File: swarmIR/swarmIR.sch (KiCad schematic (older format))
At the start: 11 parts, among them Q1 MOSFET_N, U1 TSOP1838, U2 TSOP1838, U3 TSOP1838, U4 TSOP1838

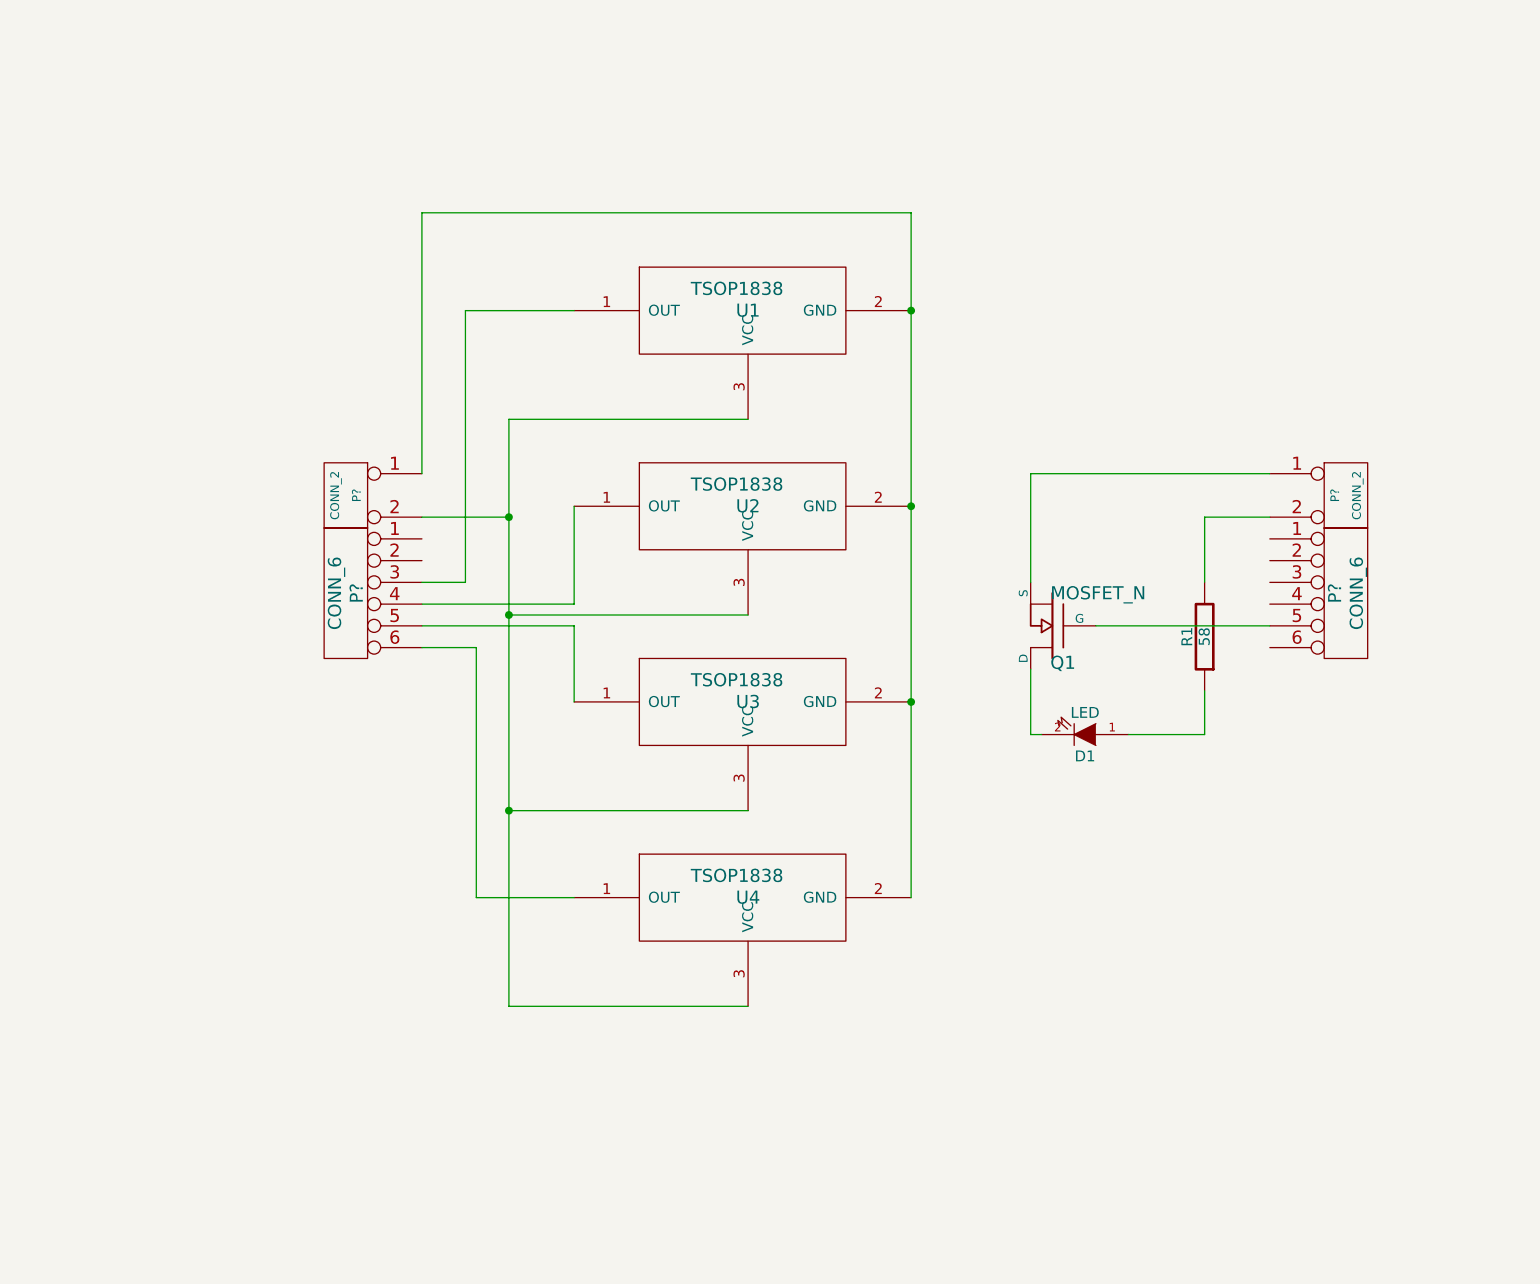
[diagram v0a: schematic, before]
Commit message: added pullups, filter cap & series R
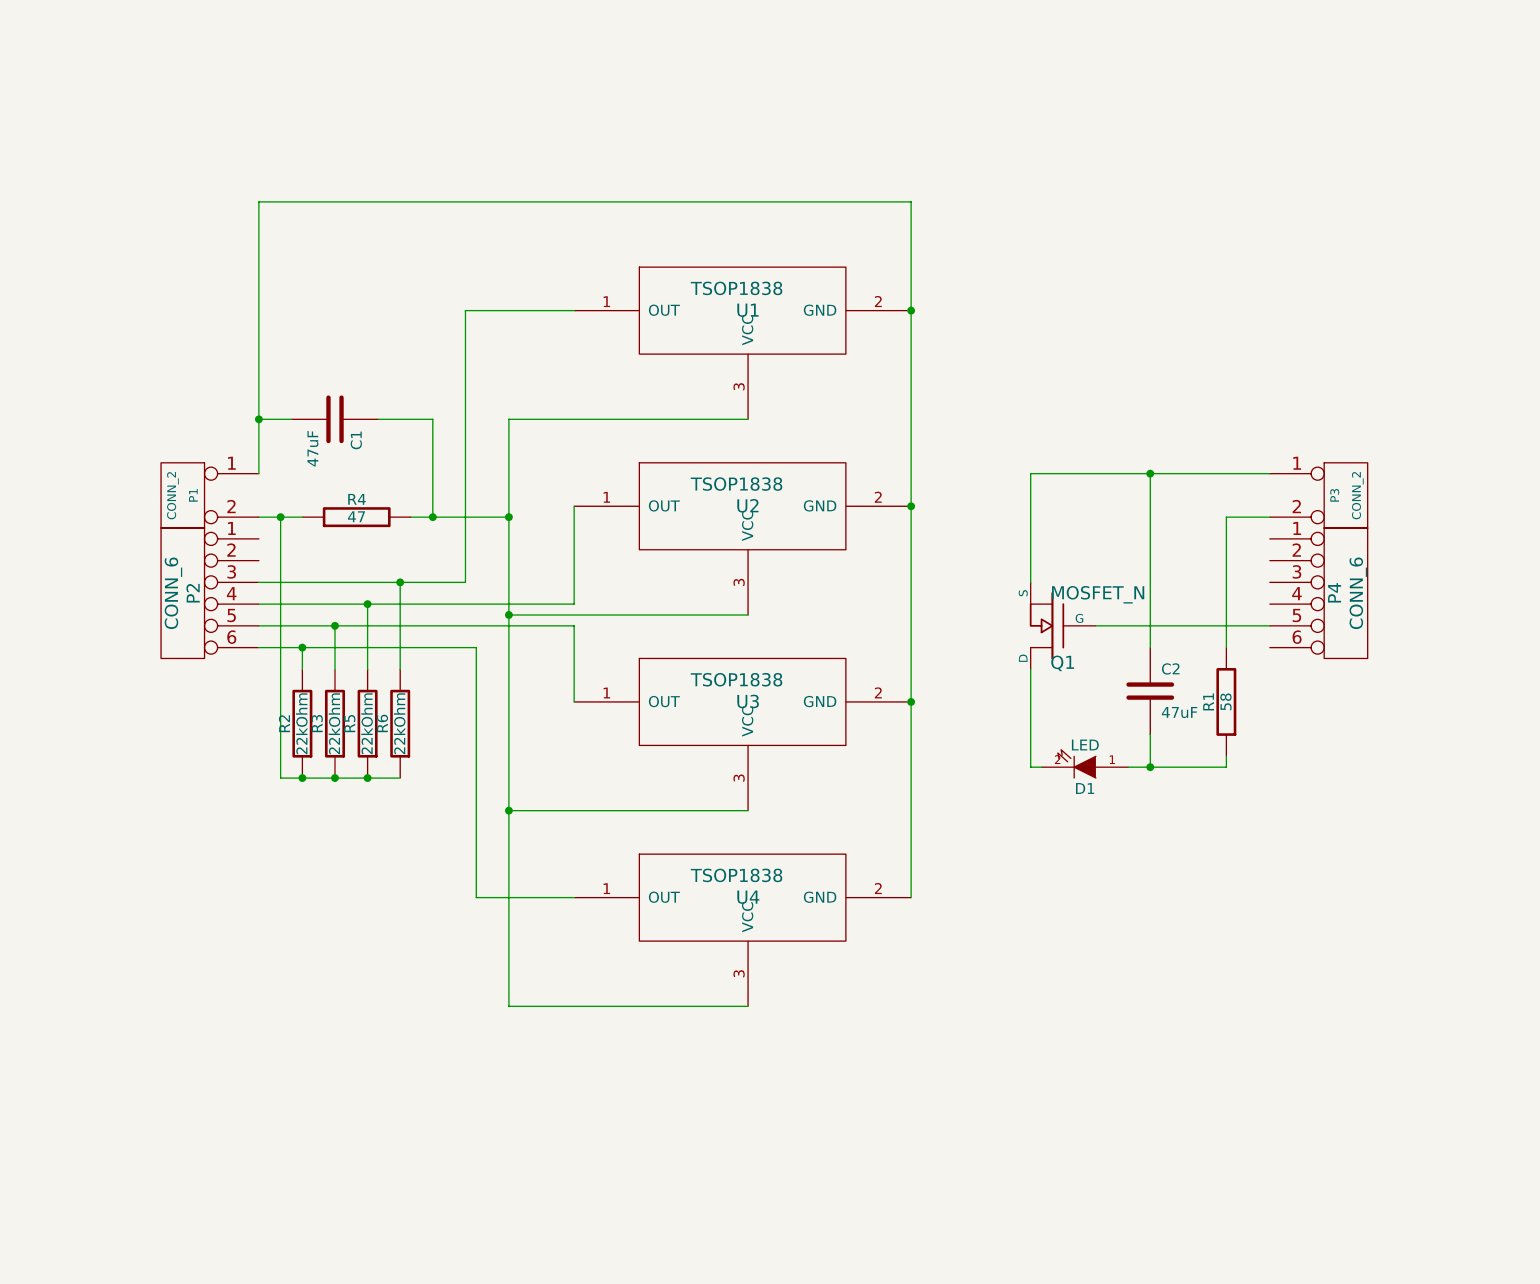
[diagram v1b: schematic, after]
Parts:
- added C1, C2: 47uF, symbol C
- added R2, R3, R5, R6: 22kOhm, symbol R
- added R4: 47, symbol R
- gave numbers to parts that had none: 4
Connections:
- net at P2.3, U1.1 (OUT): now also R6.2
- net at P1.1 (P1), U1.2 (GND), U2.2 (GND)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: now also C1.2
- net at U1.3 (VCC), U2.3 (VCC), U3.3 (VCC)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: now also C1.1, R4.2; no longer P1.2 (PM)
- net at P2.6, U4.1 (OUT): now also R2.2
- net at P2.4, U2.1 (OUT): now also R5.2
- net at P2.5, U3.1 (OUT): now also R3.2
- net at D1.1 (A), R1.1: now also C2.2
- net at P3.1 (P1), Q1.S: now also C2.1
- new net: P1.2 (PM), R2.1, R3.1, R4.1, R5.1, R6.1
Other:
- moved on the sheet: D1, P1, P2, R1
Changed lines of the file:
@@
-EESchema Schematic File Version 2  date Tue 11 Sep 2012 10:58:22 PM CST
+EESchema Schematic File Version 2  date Fri 12 Oct 2012 10:54:19 CST
 LIBS:power
 LIBS:device
@@
 LIBS:atmega32u4
 LIBS:swarmIR-cache
-EELAYER 25  0
+EELAYER 27 0
 EELAYER END
 $Descr A4 11693 8268
@@
 Sheet 1 1
 Title ""
-Date "11 sep 2012"
+Date "12 oct 2012"
 Rev ""
 Comp ""
@@
 	1    0    0    -1
 $EndComp
-Wire Wire Line
-	5850 1900 5850 5050
-Connection ~ 5850 3250
-Connection ~ 5850 4150
-Wire Wire Line
-	5100 2850 4000 2850
-Wire Wire Line
-	4000 2850 4000 5550
-Wire Wire Line
-	4000 3300 3600 3300
-Wire Wire Line
-	4000 3750 5100 3750
-Connection ~ 4000 3300
-Wire Wire Line
-	4000 4650 5100 4650
-Connection ~ 4000 3750
-Wire Wire Line
-	4000 5550 5100 5550
-Connection ~ 4000 4650
-Wire Wire Line
-	4300 2350 3800 2350
-Wire Wire Line
-	4300 3250 4300 3700
-Wire Wire Line
-	4300 5050 3850 5050
-Wire Wire Line
-	5850 1900 3600 1900
-Connection ~ 5850 2350
-Wire Wire Line
-	3800 2350 3800 3600
-Wire Wire Line
-	3800 3600 3600 3600
-Wire Wire Line
-	4300 3700 3600 3700
-Wire Wire Line
-	4300 4150 4300 3800
-Wire Wire Line
-	4300 3800 3600 3800
-Wire Wire Line
-	3850 5050 3850 3900
-Wire Wire Line
-	3850 3900 3600 3900
 $Comp
 L R R1
 U 1 1 504F4FA3
-P 7200 3850
-F 0 "R1" V 7280 3850 50  0000 C CNN
-F 1 "58" V 7200 3850 50  0000 C CNN
-	1    7200 3850
-	-1   0    0    1
-$EndComp
-Wire Wire Line
-	7500 3300 7200 3300
+P 7300 4150
+F 0 "R1" V 7380 4150 50  0000 C CNN
+F 1 "58" V 7300 4150 50  0000 C CNN
+	1    7300 4150
+	-1   0    0    1
+$EndComp
 $Comp
 L MOSFET_N Q1
@@
 	-1   0    0    1
 $EndComp
-Wire Wire Line
-	7500 3800 6700 3800
-Wire Wire Line
-	6400 3100 6400 3600
 $Comp
 L LED D1
 U 1 1 504F5090
-P 6650 4300
-F 0 "D1" H 6650 4400 50  0000 C CNN
-F 1 "LED" H 6650 4200 50  0000 C CNN
-	1    6650 4300
-	-1   0    0    1
-$EndComp
-Wire Wire Line
-	7200 3300 7200 3600
-Wire Wire Line
-	7200 4100 7200 4300
-Wire Wire Line
-	7200 4300 6850 4300
-Wire Wire Line
-	6450 4300 6400 4300
-Wire Wire Line
-	6400 4300 6400 4000
-$Comp
-L CONN_2 P?
+P 6650 4450
+F 0 "D1" H 6650 4550 50  0000 C CNN
+F 1 "LED" H 6650 4350 50  0000 C CNN
+	1    6650 4450
+	-1   0    0    1
+$EndComp
+$Comp
+L CONN_2 P1
 U 1 1 504F51BC
-P 3250 3200
-F 0 "P?" V 3200 3200 40  0000 C CNN
-F 1 "CONN_2" V 3300 3200 40  0000 C CNN
-	1    3250 3200
+P 2500 3200
+F 0 "P1" V 2450 3200 40  0000 C CNN
+F 1 "CONN_2" V 2550 3200 40  0000 C CNN
+	1    2500 3200
 	-1   0    0    -1
 $EndComp
 $Comp
-L CONN_2 P?
+L CONN_2 P3
 U 1 1 504F51CB
 P 7850 3200
-F 0 "P?" V 7800 3200 40  0000 C CNN
+F 0 "P3" V 7800 3200 40  0000 C CNN
 F 1 "CONN_2" V 7900 3200 40  0000 C CNN
 	1    7850 3200
@@
 $EndComp
 $Comp
-L CONN_6 P?
+L CONN_6 P2
 U 1 1 504F51DA
-P 3250 3650
-F 0 "P?" V 3200 3650 60  0000 C CNN
-F 1 "CONN_6" V 3300 3650 60  0000 C CNN
-	1    3250 3650
+P 2500 3650
+F 0 "P2" V 2450 3650 60  0000 C CNN
+F 1 "CONN_6" V 2550 3650 60  0000 C CNN
+	1    2500 3650
 	-1   0    0    -1
 $EndComp
 $Comp
-L CONN_6 P?
+L CONN_6 P4
 U 1 1 504F51E9
 P 7850 3650
-F 0 "P?" V 7800 3650 60  0000 C CNN
+F 0 "P4" V 7800 3650 60  0000 C CNN
 F 1 "CONN_6" V 7900 3650 60  0000 C CNN
 	1    7850 3650
 	1    0    0    -1
 $EndComp
-Wire Wire Line
-	3600 1900 3600 3100
+$Comp
+L R R4
+U 1 1 507781A3
+P 3300 3300
+F 0 "R4" V 3380 3300 50  0000 C CNN
+F 1 "47" V 3300 3300 50  0000 C CNN
+	1    3300 3300
+	0    -1   -1   0
+$EndComp
+$Comp
+L C C1
+U 1 1 507782FA
+P 3200 2850
+F 0 "C1" H 3250 2950 50  0000 L CNN
+F 1 "47uF" H 3250 2750 50  0000 L CNN
+	1    3200 2850
+	0    1    1    0
+$EndComp
+$Comp
+L C C2
+U 1 1 50778457
+P 6950 4100
+F 0 "C2" H 7000 4200 50  0000 L CNN
+F 1 "47uF" H 7000 4000 50  0000 L CNN
+	1    6950 4100
+	1    0    0    -1
+$EndComp
+$Comp
+L R R2
+U 1 1 5077853E
+P 3050 4250
+F 0 "R2" V 3130 4250 50  0000 C CNN
+F 1 "22kOhm" V 3050 4250 50  0000 C CNN
+	1    3050 4250
+	-1   0    0    1
+$EndComp
+$Comp
+L R R3
+U 1 1 5077859F
+P 3200 4250
+F 0 "R3" V 3280 4250 50  0000 C CNN
+F 1 "22kOhm" V 3200 4250 50  0000 C CNN
+	1    3200 4250
+	-1   0    0    1
+$EndComp
+$Comp
+L R R5
+U 1 1 507785A7
+P 3350 4250
+F 0 "R5" V 3430 4250 50  0000 C CNN
+F 1 "22kOhm" V 3350 4250 50  0000 C CNN
+	1    3350 4250
+	-1   0    0    1
+$EndComp
+$Comp
+L R R6
+U 1 1 507785AD
+P 3500 4250
+F 0 "R6" V 3580 4250 50  0000 C CNN
+F 1 "22kOhm" V 3500 4250 50  0000 C CNN
+	1    3500 4250
+	-1   0    0    1
+$EndComp
+Connection ~ 5850 3250
+Connection ~ 5850 4150
+Wire Wire Line
+	5100 2850 4000 2850
+Wire Wire Line
+	4000 2850 4000 5550
+Wire Wire Line
+	3550 3300 4000 3300
+Wire Wire Line
+	4000 3750 5100 3750
+Connection ~ 4000 3300
+Wire Wire Line
+	4000 4650 5100 4650
+Connection ~ 4000 3750
+Wire Wire Line
+	4000 5550 5100 5550
+Connection ~ 4000 4650
+Wire Wire Line
+	4300 2350 3800 2350
+Wire Wire Line
+	4300 3700 4300 3250
+Wire Wire Line
+	4300 5050 3850 5050
+Connection ~ 5850 2350
+Wire Wire Line
+	3800 2350 3800 3600
+Wire Wire Line
+	3800 3600 2850 3600
+Wire Wire Line
+	2850 3700 4300 3700
+Wire Wire Line
+	4300 3800 4300 4150
+Wire Wire Line
+	2850 3800 4300 3800
+Wire Wire Line
+	3850 5050 3850 3900
+Wire Wire Line
+	3850 3900 2850 3900
+Wire Wire Line
+	7500 3800 6700 3800
+Wire Wire Line
+	6400 3100 6400 3600
 Wire Wire Line
 	6400 3100 7500 3100
+Wire Wire Line
+	5850 1850 5850 5050
+Wire Wire Line
+	5850 1850 2850 1850
+Wire Wire Line
+	2850 1850 2850 3100
+Wire Wire Line
+	3050 3300 2850 3300
+Wire Wire Line
+	3400 2850 3650 2850
+Wire Wire Line
+	3650 2850 3650 3300
+Connection ~ 3650 3300
+Wire Wire Line
+	3000 2850 2850 2850
+Connection ~ 2850 2850
+Wire Wire Line
+	7500 3300 7300 3300
+Wire Wire Line
+	7300 3300 7300 3900
+Wire Wire Line
+	7300 4450 7300 4400
+Wire Wire Line
+	6850 4450 7300 4450
+Wire Wire Line
+	6450 4450 6400 4450
+Wire Wire Line
+	6400 4450 6400 4000
+Wire Wire Line
+	6950 3900 6950 3100
+Connection ~ 6950 3100
+Wire Wire Line
+	6950 4300 6950 4450
+Connection ~ 6950 4450
+Wire Wire Line
+	2950 4500 3500 4500
+Connection ~ 3350 4500
+Connection ~ 3200 4500
+Wire Wire Line
+	2950 4500 2950 3300
+Connection ~ 2950 3300
+Connection ~ 3050 4500
+Wire Wire Line
+	3050 3900 3050 4000
+Connection ~ 3050 3900
+Wire Wire Line
+	3200 4000 3200 3800
+Connection ~ 3200 3800
+Wire Wire Line
+	3350 4000 3350 3700
+Connection ~ 3350 3700
+Wire Wire Line
+	3500 4000 3500 3600
+Connection ~ 3500 3600
 $EndSCHEMATC
